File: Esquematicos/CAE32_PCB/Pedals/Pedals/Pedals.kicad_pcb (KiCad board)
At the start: 4 copper layers, 76.1 x 70.2 mm, 134 parts, among them J1 SPI_MASTER, J10 Conn_01x03_Female, J11 Conn_01x03_Female, J12 Conn_01x03_Female, J13 Conn_01x03_Female, J14 Conn_01x03_Female, J15 USB_C_Receptacle_USB2.0, J16 UART_PGR, J17 ST-Link, J18 LC_2, J19 LC_1, J2 CAN, J20 LC_3, J3 PGRM and SPI, J4 Conn_01x03_Female, J5 Conn_01x03_Female, J6 Conn_01x03_Female, J7 Conn_01x03_Female, J8 Conn_01x03_Female, J9 Conn_01x03_Female, Q1 MMBT3906, Q2 MMBT3906, Q3 MMBT3906, SW1 CONFIG, SW2 BOOT, SW3 RST, U1 STM32F072RBTx, U2 REF3033, U3 ADC128S102, U4 LDL1117, U5 HX711, U6 HX711, U7 HX711

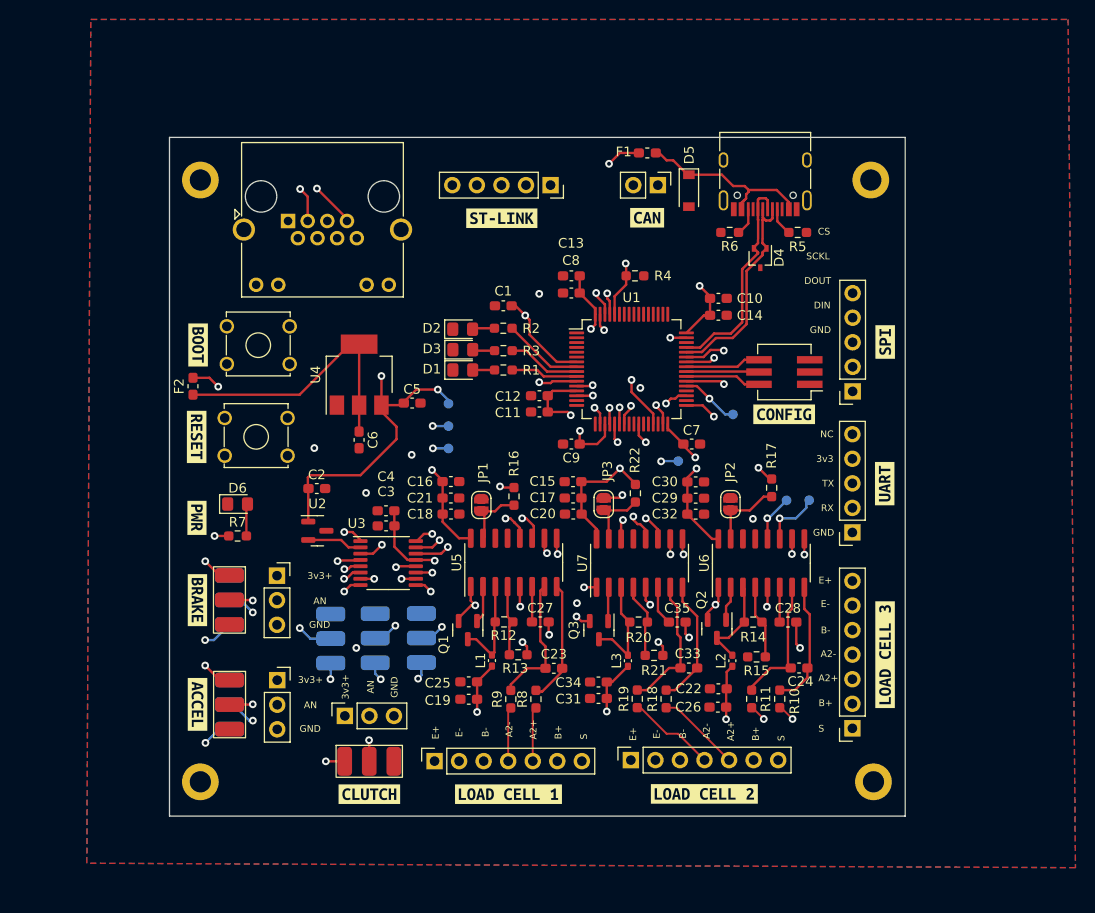
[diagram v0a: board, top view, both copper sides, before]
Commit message: update: se agrega via stitching a la pcb de los pedales
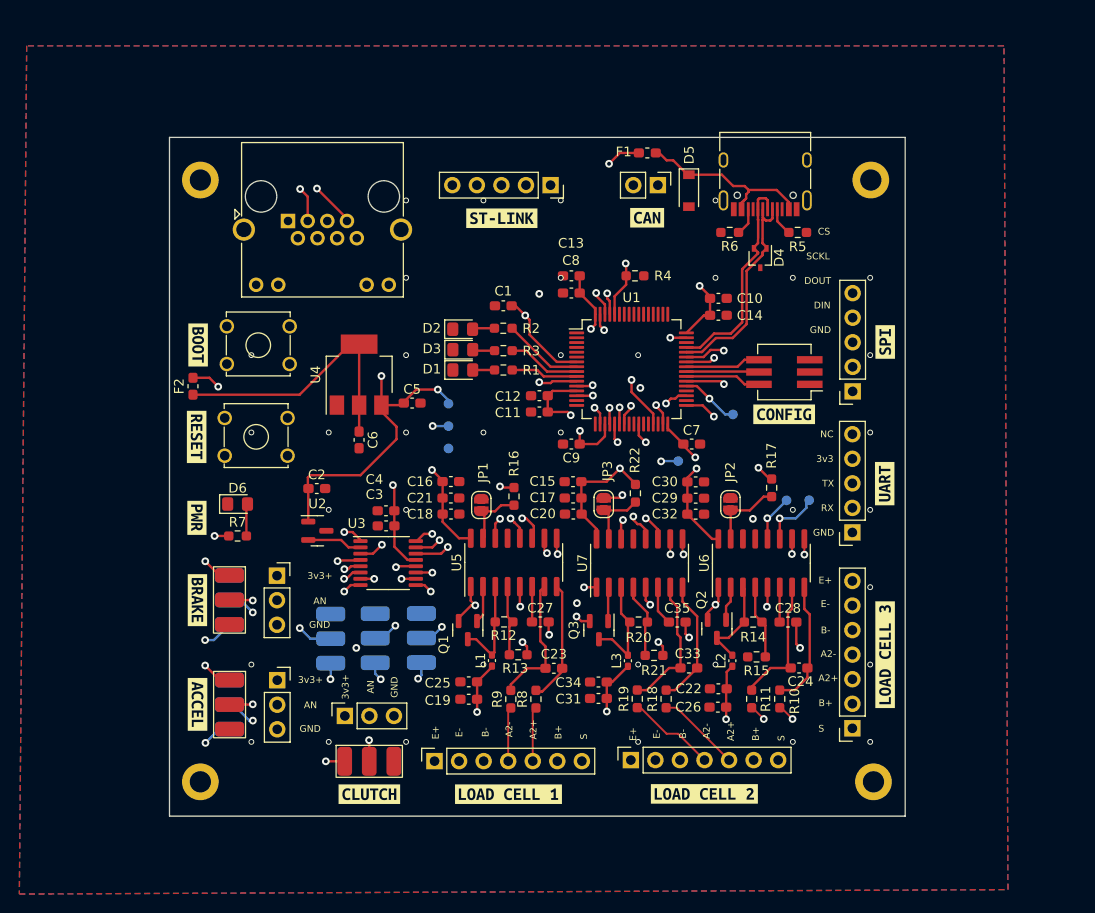
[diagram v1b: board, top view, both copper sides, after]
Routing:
- net /LOAD_CELL_2: track 37.2 -> 36.5 mm
- net +3.3V: track 112.3 -> 113.0 mm
- net GNDREF: track 34.9 -> 35.5 mm, vias 23 -> 56
